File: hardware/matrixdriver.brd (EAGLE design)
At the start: 50 x 50 mm, 47 parts, among them IC1 75176AD, IC2 4017D, IC3 ULN2803, IC4 7805DT, Q1 20MHZ, Q2 MMBT4403LT1SMD, Q3 MMBT4403LT1SMD, Q4 MMBT4403LT1SMD, Q5 MMBT4403LT1SMD, Q6 MMBT4403LT1SMD, Q7 MMBT4403LT1SMD, Q8 MMBT4403LT1SMD, Q9 MMBT4403LT1SMD

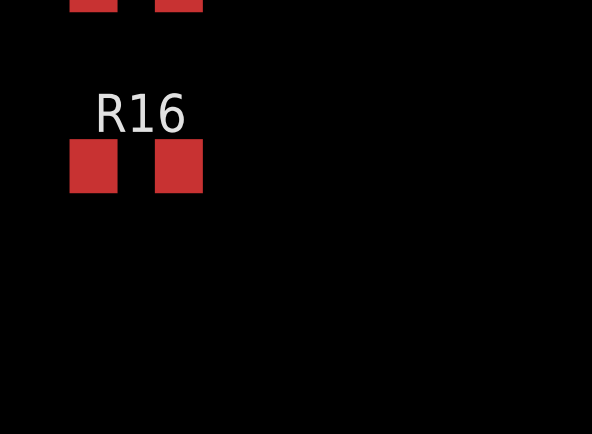
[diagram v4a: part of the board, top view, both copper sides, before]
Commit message: working on Hardware Revision 2 - fix pullup
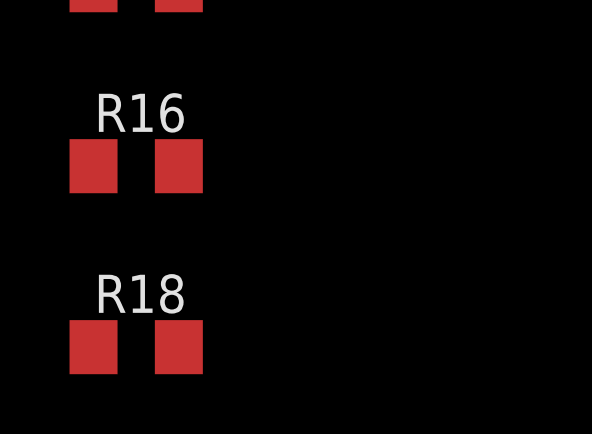
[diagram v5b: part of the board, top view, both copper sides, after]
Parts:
- added R18: 10k, resistor:R1206
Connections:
- removed net N$461: TP2.TP
- net N$59: now also R18.1
- net VCC: now also R18.2, TP2.TP
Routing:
- net VCC: track 0.00 -> 11.0 mm
- net N$461: track 11.0 -> 0.00 mm
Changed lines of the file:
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@@
 <element name="R15" library="resistor" package="R1206" value="10" x="2.54" y="-93.345"/>
 <element name="R16" library="resistor" package="R1206" value="10" x="2.54" y="-99.3775"/>
+<element name="R18" library="resistor" package="R1206" value="10k" x="2.54" y="-105.41"/>
 </elements>
 <signals>
@@
 <wire x1="6.6675" y1="9.525" x2="6.985" y2="9.8425" width="0.4064" layer="1"/>
 <wire x1="6.985" y1="9.8425" x2="6.985" y2="11.2395" width="0.4064" layer="1"/>
-</signal>
-<signal name="N$461">
-<wire x1="9.205" y1="32.065" x2="9.525" y2="32.385" width="0.4064" layer="1"/>
-<wire x1="9.525" y1="32.385" x2="11.915" y2="32.385" width="0.4064" layer="1"/>
-<contactref element="TP2" pad="TP"/>
-<wire x1="1.6764" y1="31.75" x2="3.81" y2="31.75" width="0.4064" layer="1"/>
-<wire x1="3.81" y1="31.75" x2="4.445" y2="32.385" width="0.4064" layer="1"/>
-<wire x1="4.445" y1="32.385" x2="9.525" y2="32.385" width="0.4064" layer="1"/>
 </signal>
 <signal name="GND" class="2">
@@
 <wire x1="6.35" y1="13.335" x2="5.715" y2="12.7" width="0.4064" layer="1"/>
 <wire x1="5.715" y1="12.7" x2="5.715" y2="11.2395" width="0.4064" layer="1"/>
+<contactref element="R18" pad="1"/>
+<wire x1="5.715" y1="11.2395" x2="1.118" y2="-105.41" width="0" layer="19" extent="1-1"/>
 </signal>
 <signal name="N$60">
@@
 <contactref element="R12" pad="2"/>
 <contactref element="R10" pad="2"/>
-<contactref element="R13" pad="2"/>
 <contactref element="R11" pad="2"/>
 <contactref element="R14" pad="2"/>
@@
 <contactref element="IC4" pad="2"/>
 <contactref element="IC2" pad="16"/>
+<wire x1="9.205" y1="32.065" x2="9.525" y2="32.385" width="0.4064" layer="1"/>
+<wire x1="9.525" y1="32.385" x2="11.915" y2="32.385" width="0.4064" layer="1"/>
+<contactref element="TP2" pad="TP"/>
+<wire x1="1.6764" y1="31.75" x2="3.81" y2="31.75" width="0.4064" layer="1"/>
+<wire x1="3.81" y1="31.75" x2="4.445" y2="32.385" width="0.4064" layer="1"/>
+<wire x1="4.445" y1="32.385" x2="9.525" y2="32.385" width="0.4064" layer="1"/>
+<contactref element="R18" pad="2"/>
+<contactref element="R13" pad="2"/>
+<wire x1="3.962" y1="-99.3775" x2="3.962" y2="-105.41" width="0" layer="19" extent="1-1"/>
 <wire x1="3.962" y1="-93.345" x2="3.962" y2="-99.3775" width="0" layer="19" extent="1-1"/>
 <wire x1="3.962" y1="-87.3125" x2="3.962" y2="-93.345" width="0" layer="19" extent="1-1"/>
@@
 <wire x1="2.54" y1="14.1" x2="3.962" y2="-57.15" width="0" layer="19" extent="1-1"/>
 <wire x1="5.715" y1="20.5105" x2="2.54" y2="14.1" width="0" layer="19" extent="1-1"/>
-<wire x1="30.48" y1="18.5166" x2="5.715" y2="20.5105" width="0" layer="19" extent="1-1"/>
+<wire x1="3.81" y1="31.75" x2="5.715" y2="20.5105" width="0" layer="19" extent="1-1"/>
+<wire x1="30.48" y1="18.5166" x2="11.915" y2="32.385" width="0" layer="19" extent="1-1"/>
 <wire x1="32.385" y1="15.45" x2="30.48" y2="18.5166" width="0" layer="19" extent="1-1"/>
 <wire x1="34.925" y1="9.95" x2="32.385" y2="15.45" width="0" layer="19" extent="1-1"/>

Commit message: work on schematics
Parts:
- added C3, C7: 100n, rcl:C1206
- C4: value 10µ -> 100n
- C6: value 100UF -> 10UF
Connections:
- new net N$36: C4.1, IC4.2
- net GND: now also C3.2, C7.2
- net N$65: now also C3.1
- net VCC: now also C7.1; no longer C4.1, IC4.2
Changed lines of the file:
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@@
 <attribute name="VALUE" x="48.5775" y="35.56" size="1.27" layer="27" rot="R180"/>
 </element>
-<element name="C4" library="rcl" package="C1206" value="10µ" x="45.085" y="17.78" smashed="yes">
+<element name="C4" library="rcl" package="C1206" value="100n" x="45.085" y="17.78" smashed="yes">
 <attribute name="VALUE" x="49.2125" y="16.51" size="1.27" layer="27" rot="R90"/>
 </element>
@@
 <attribute name="VALUE" x="5.588" y="13.0175" size="1.27" layer="27" rot="R90"/>
 </element>
-<element name="C6" library="Panasonic-EEEFT_EEEH" package="CAPAE660X800N" value="100UF" x="43.18" y="12.065" smashed="yes">
+<element name="C6" library="Panasonic-EEEFT_EEEH" package="CAPAE660X800N" value="10UF" x="43.18" y="12.065" smashed="yes">
 <attribute name="PACKAGE" value="CASE-D8" x="43.18" y="12.065" size="1.778" layer="27" display="off"/>
 <attribute name="OC_NEWARK" value="15R0909" x="43.18" y="12.065" size="1.778" layer="27" display="off"/>
@@
 <element name="R16" library="resistor" package="R1206" value="10" x="2.54" y="-99.3775"/>
 <element name="R18" library="resistor" package="R1206" value="10k" x="2.54" y="-105.41"/>
+<element name="C3" library="rcl" package="C1206" value="100n" x="2.54" y="-111.4425"/>
+<element name="C7" library="rcl" package="C1206" value="100n" x="2.54" y="-117.475"/>
 </elements>
 <signals>
@@
 </polygon>
 <contactref element="U$2" pad="CASE"/>
+<contactref element="C3" pad="2"/>
+<contactref element="C7" pad="2"/>
+<wire x1="3.94" y1="-111.4425" x2="3.94" y2="-117.475" width="0" layer="19" extent="1-1"/>
+<wire x1="6.985" y1="3.68" x2="3.94" y2="-111.4425" width="0" layer="19" extent="1-1"/>
+<wire x1="2.54" y1="7.9375" x2="6.985" y2="3.68" width="0" layer="19" extent="1-1"/>
+<wire x1="2.54" y1="11.3" x2="2.54" y2="7.9375" width="0" layer="19" extent="1-1"/>
+<wire x1="8.89" y1="13.6525" x2="2.54" y2="11.3" width="0" layer="19" extent="1-1"/>
+<wire x1="10.795" y1="17.78" x2="8.89" y2="13.6525" width="0" layer="19" extent="1-1"/>
+<wire x1="17.145" y1="11.2395" x2="8.89" y2="13.6525" width="0" layer="19" extent="1-1"/>
+<wire x1="19.685" y1="10.4775" x2="17.145" y2="11.2395" width="0" layer="19" extent="1-1"/>
+<wire x1="22.225" y1="10.795" x2="19.685" y2="10.4775" width="0" layer="19" extent="1-1"/>
+<wire x1="24.765" y1="10.795" x2="22.225" y2="10.795" width="0" layer="19" extent="1-1"/>
+<wire x1="27.305" y1="10.795" x2="24.765" y2="10.795" width="0" layer="19" extent="1-1"/>
+<wire x1="30.1625" y1="9.525" x2="27.305" y2="10.795" width="0" layer="19" extent="1-1"/>
+<wire x1="29.845" y1="15.392" x2="27.305" y2="10.795" width="0" layer="19" extent="1-1"/>
+<wire x1="26.67" y1="18.5166" x2="29.845" y2="15.392" width="0" layer="19" extent="1-1"/>
+<wire x1="27.305" y1="5.08" x2="30.1625" y2="9.525" width="0" layer="19" extent="1-1"/>
+<wire x1="24.765" y1="3.68" x2="27.305" y2="5.08" width="0" layer="19" extent="1-1"/>
+<wire x1="36.195" y1="15.45" x2="29.845" y2="15.392" width="0" layer="19" extent="1-1"/>
+<wire x1="39.37" y1="15.24" x2="36.195" y2="15.45" width="0" layer="19" extent="1-1"/>
+<wire x1="40.64" y1="19.05" x2="39.37" y2="15.24" width="0" layer="19" extent="1-1"/>
+<wire x1="46.485" y1="17.78" x2="40.64" y2="19.05" width="0" layer="19" extent="1-1"/>
+<wire x1="47.9425" y1="21.9075" x2="46.485" y2="17.78" width="0" layer="19" extent="1-1"/>
+<wire x1="46.18" y1="24.765" x2="47.9425" y2="21.9075" width="0" layer="19" extent="1-1"/>
+<wire x1="42.545" y1="26.67" x2="46.18" y2="24.765" width="0" layer="19" extent="1-1"/>
+<wire x1="43.18" y1="29.465" x2="42.545" y2="26.67" width="0" layer="19" extent="1-1"/>
+<wire x1="41.275" y1="31.8008" x2="43.18" y2="29.465" width="0" layer="19" extent="1-1"/>
+<wire x1="45.72" y1="32.0675" x2="43.18" y2="29.465" width="0" layer="19" extent="1-1"/>
+<wire x1="48.5775" y1="28.575" x2="46.18" y2="24.765" width="0" layer="19" extent="1-1"/>
+<wire x1="39.6875" y1="36.195" x2="41.275" y2="31.8008" width="0" layer="19" extent="1-1"/>
+<wire x1="45.593" y1="12.065" x2="46.485" y2="17.78" width="0" layer="19" extent="1-1"/>
+<wire x1="33.9725" y1="39.6875" x2="39.6875" y2="36.195" width="0" layer="19" extent="1-1"/>
+<wire x1="32.385" y1="45.085" x2="33.9725" y2="39.6875" width="0" layer="19" extent="1-1"/>
+<wire x1="29.21" y1="43.4975" x2="32.385" y2="45.085" width="0" layer="19" extent="1-1"/>
+<wire x1="45.085" y1="5.08" x2="45.593" y2="12.065" width="0" layer="19" extent="1-1"/>
+<wire x1="35.56" y1="24.13" x2="40.64" y2="19.05" width="0" layer="19" extent="1-1"/>
+<wire x1="34.925" y1="27.305" x2="35.56" y2="24.13" width="0" layer="19" extent="1-1"/>
+<wire x1="46.355" y1="39.33" x2="45.72" y2="32.0675" width="0" layer="19" extent="1-1"/>
+<wire x1="46.355" y1="44.1325" x2="46.355" y2="39.33" width="0" layer="19" extent="1-1"/>
+<wire x1="36.195" y1="5.08" x2="30.1625" y2="9.525" width="0" layer="19" extent="1-1"/>
+<wire x1="21.59" y1="24.6634" x2="26.67" y2="18.5166" width="0" layer="19" extent="1-1"/>
+<wire x1="21.59" y1="27.305" x2="21.59" y2="24.6634" width="0" layer="19" extent="1-1"/>
+<wire x1="25.4" y1="26.9875" x2="21.59" y2="27.305" width="0" layer="19" extent="1-1"/>
+<wire x1="19.05" y1="20.955" x2="21.59" y2="24.6634" width="0" layer="19" extent="1-1"/>
+<wire x1="18.0975" y1="30.1625" x2="21.59" y2="27.305" width="0" layer="19" extent="1-1"/>
+<wire x1="22.86" y1="33.655" x2="18.0975" y2="30.1625" width="0" layer="19" extent="1-1"/>
+<wire x1="24.13" y1="36.195" x2="22.86" y2="33.655" width="0" layer="19" extent="1-1"/>
+<wire x1="18.0975" y1="38.1" x2="24.13" y2="36.195" width="0" layer="19" extent="1-1"/>
+<wire x1="10.16" y1="33.655" x2="18.0975" y2="30.1625" width="0" layer="19" extent="1-1"/>
+<wire x1="6.6675" y1="39.37" x2="10.16" y2="33.655" width="0" layer="19" extent="1-1"/>
+<wire x1="3.81" y1="30.48" x2="10.16" y2="33.655" width="0" layer="19" extent="1-1"/>
+<wire x1="3.81" y1="27.94" x2="3.81" y2="30.48" width="0" layer="19" extent="1-1"/>
+<wire x1="3.81" y1="25.4" x2="3.81" y2="27.94" width="0" layer="19" extent="1-1"/>
+<wire x1="1.7272" y1="21.59" x2="3.81" y2="25.4" width="0" layer="19" extent="1-1"/>
 </signal>
 <signal name="N$15">
@@
 <wire x1="42.9" y1="32.03" x2="42.8625" y2="32.0675" width="0.4064" layer="1"/>
 <via x="41.91" y="23.035" extent="1-16" drill="0.6"/>
+<contactref element="C3" pad="1"/>
+<wire x1="40.767" y1="12.065" x2="1.14" y2="-111.4425" width="0" layer="19" extent="1-1"/>
 </signal>
 <signal name="N$11">
@@
 <contactref element="U$1" pad="20"/>
 <contactref element="C5" pad="2"/>
-<contactref element="C4" pad="1"/>
-<contactref element="IC4" pad="2"/>
 <contactref element="IC2" pad="16"/>
 <wire x1="9.205" y1="32.065" x2="9.525" y2="32.385" width="0.4064" layer="1"/>
@@
 <contactref element="R18" pad="2"/>
 <contactref element="R13" pad="2"/>
+<contactref element="C7" pad="1"/>
+<wire x1="3.962" y1="-105.41" x2="1.14" y2="-117.475" width="0" layer="19" extent="1-1"/>
 <wire x1="3.962" y1="-99.3775" x2="3.962" y2="-105.41" width="0" layer="19" extent="1-1"/>
 <wire x1="3.962" y1="-93.345" x2="3.962" y2="-99.3775" width="0" layer="19" extent="1-1"/>
@@
 <wire x1="32.385" y1="15.45" x2="30.48" y2="18.5166" width="0" layer="19" extent="1-1"/>
 <wire x1="34.925" y1="9.95" x2="32.385" y2="15.45" width="0" layer="19" extent="1-1"/>
-<wire x1="43.685" y1="17.78" x2="32.385" y2="15.45" width="0" layer="19" extent="1-1"/>
-<wire x1="48.635" y1="32.03" x2="43.685" y2="17.78" width="0" layer="19" extent="1-1"/>
 </signal>
 <signal name="N$34">
@@
 <wire x1="21.905" y1="31.285" x2="1.118" y2="-93.345" width="0" layer="19" extent="1-1"/>
 </signal>
+<signal name="N$36">
+<contactref element="C4" pad="1"/>
+<contactref element="IC4" pad="2"/>
+<wire x1="43.685" y1="17.78" x2="48.635" y2="32.03" width="0" layer="19" extent="1-1"/>
+</signal>
 </signals>
